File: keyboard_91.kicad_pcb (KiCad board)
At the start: 2 copper layers, 210 x 113 mm, 52 parts, among them J1 SW_Cherry_MX_1.00u_Plate, K1 SW_Cherry_MX_1.00u_Plate, M1 SW_Cherry_MX_1.00u_Plate, P1 SW_Cherry_MX_1.00u_Plate, Q1 SW_Cherry_MX_1.00u_Plate, T1 SW_Cherry_MX_1.00u_Plate, U1 SW_Cherry_MX_1.00u_Plate, X1 SW_Cherry_MX_1.00u_Plate, Y1 SW_Cherry_MX_1.00u_Plate

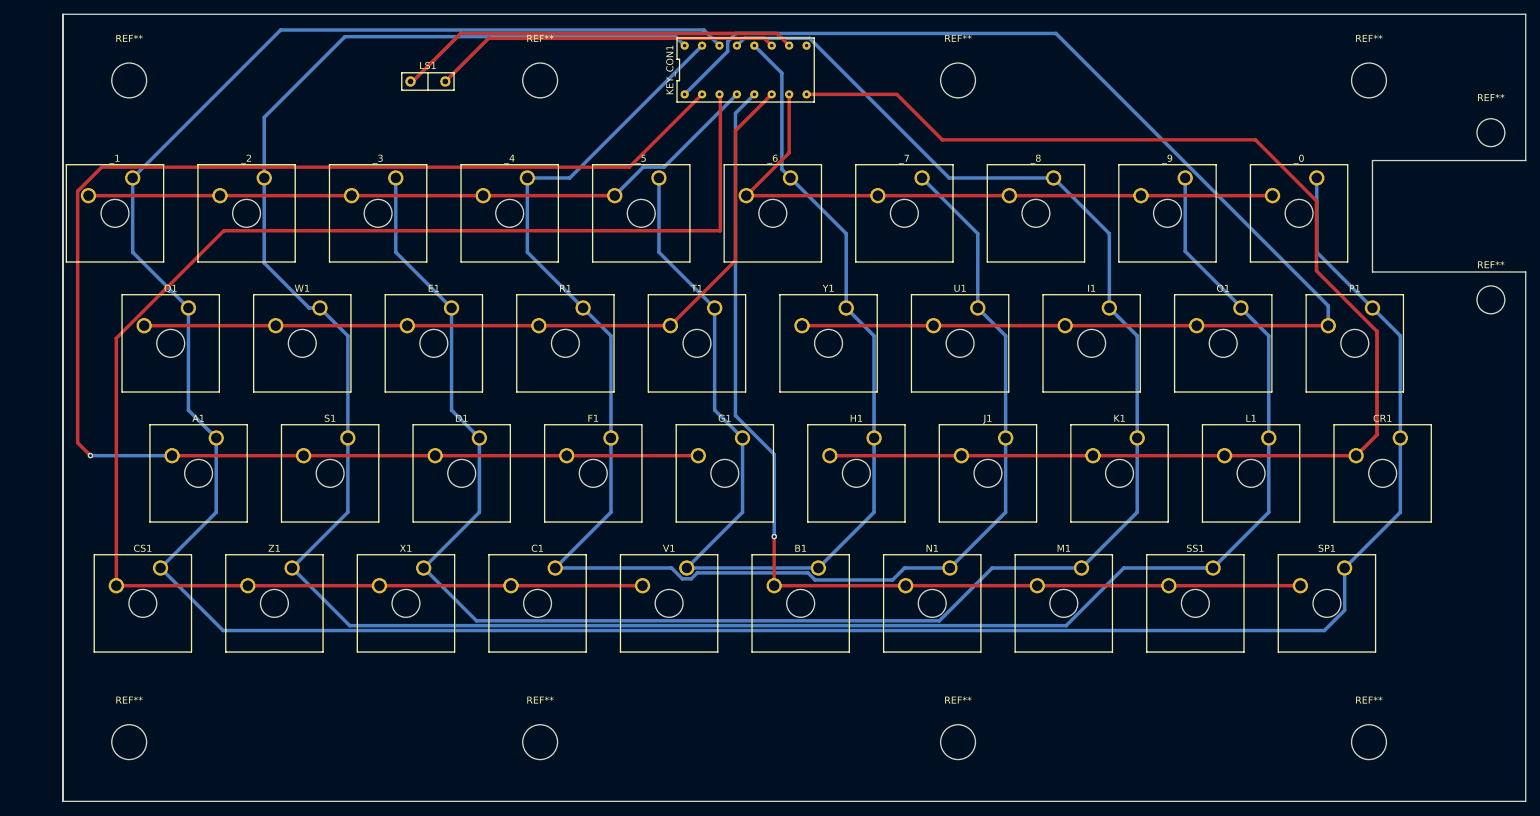
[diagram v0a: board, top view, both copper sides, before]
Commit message: Moure touches
- hide useless stuff
- add reset buttons SIP
- add speaker SIP
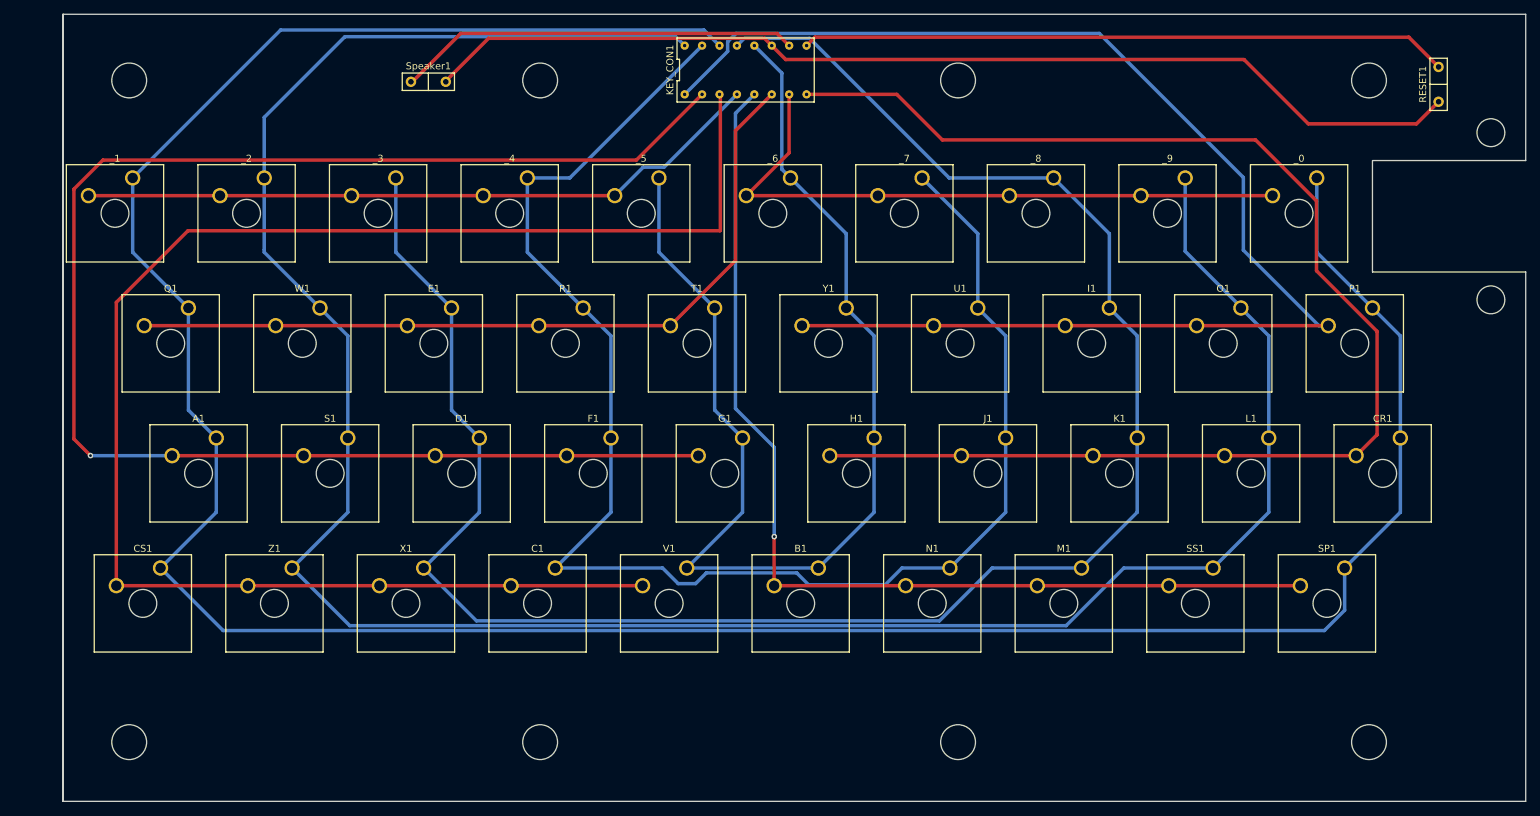
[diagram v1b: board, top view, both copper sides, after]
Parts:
- removed LS1: Speaker, Library:SIP-2
- added RESET1: RESET, Library:SIP-2, F.Cu at (217.5, 30.1)
- added Speaker1: Speaker, Library:SIP-2, F.Cu at (72.5, 29.7)
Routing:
- net /GND: track 49.9 -> 151.6 mm
- net /RST: track 0.00 -> 93.0 mm
- net /K_Y-P: track 191.4 -> 195.9 mm
- net /K_CS-V: track 223.8 -> 226.8 mm
- net /K_4-C_N-7: track 220.3 -> 221.5 mm
- net /K_A-G: track 221.4 -> 222.3 mm
- net /K_2-Z_SS-9: track 342.9 -> 342.0 mm
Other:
- board text added: "HC 85/90/91 Cherry MX PCB V1"
- board text added: "https://zx.licentia.eu"

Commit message: Second try
- fixed cherry mx holes (make them 0.8 mm)
- fixed connector holes
- fixed  sound & reset holes
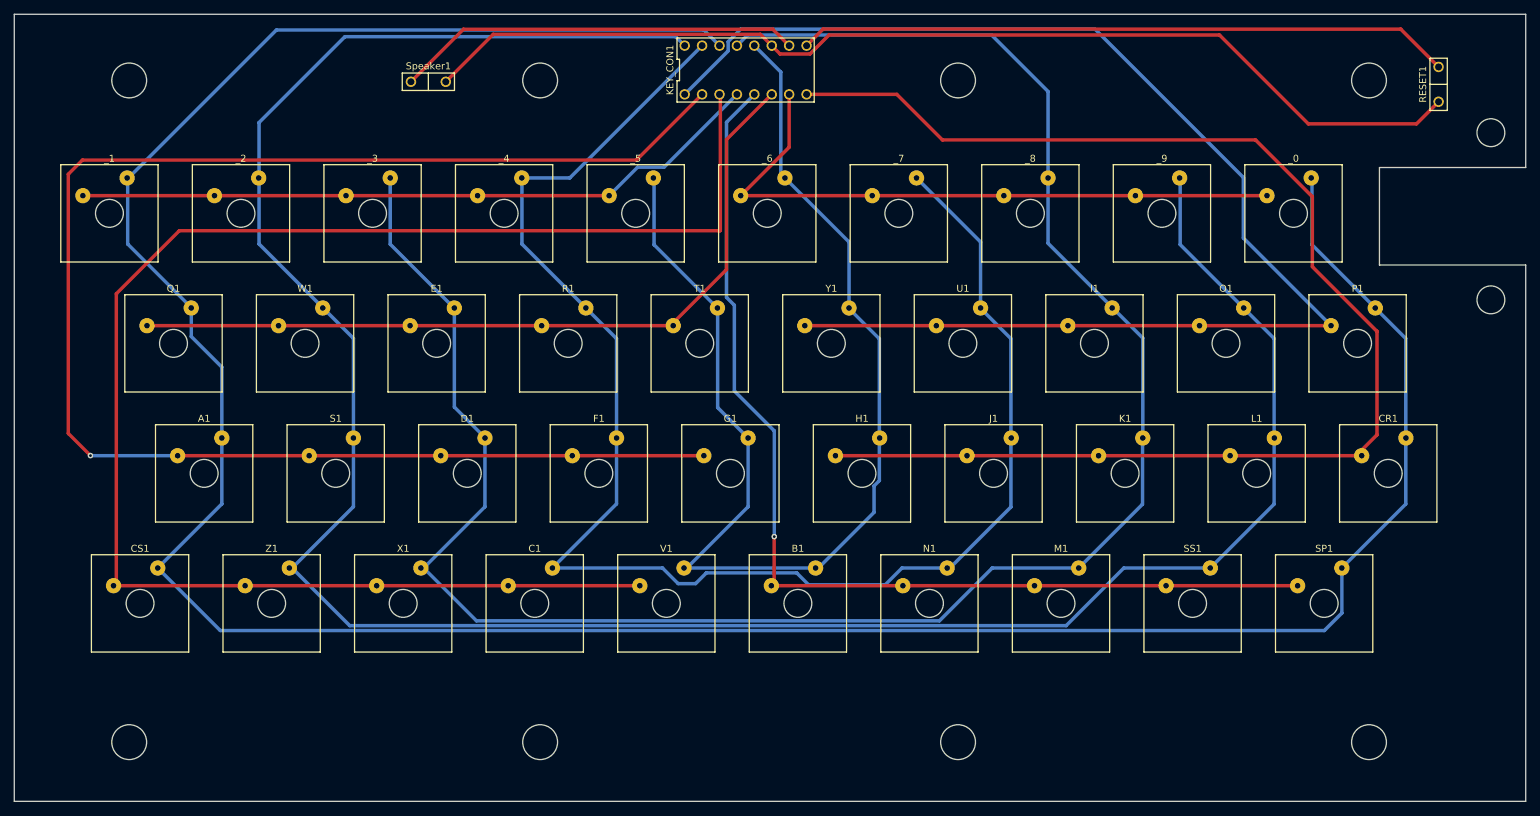
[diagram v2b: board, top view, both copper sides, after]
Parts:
- A1, B1, C1, CR1, CS1, D1, E1, F1, G1, H1, I1, J1, K1, L1, M1, N1, O1, P1, Q1, R1, S1, SP1, SS1, T1, U1, V1, W1, X1, Y1, Z1, _0, _1, _2, _3, _4, _5, _6, _7, _8, _9: value SW_Cherry_MX_1.00u_Plate -> SW_Cherry_MX_0.80u_Plate; footprint Button_Switch_Keyboard:SW_Cherry_MX_1.00u_Plate -> Library:SW_Cherry_MX_0.80u_Plate
- moved CR1 0.80 mm to (212.8, 80.8)
- moved H1 0.80 mm to (137.2, 80.8)
- moved J1 0.80 mm to (156.1, 80.8)
- moved _5 0.80 mm to (104.8, 43.5)
- moved _8 0.80 mm to (161.4, 43.5)
- moved _9 0.80 mm to (180.3, 43.5)
- moved _2 0.80 mm to (48.1, 43.5)
- moved _1 0.80 mm to (29.2, 43.5)
- moved A1 0.80 mm to (42.8, 80.8)
- moved D1 0.80 mm to (80.6, 80.8)
- moved F1 0.80 mm to (99.5, 80.8)
- moved G1 0.80 mm to (118.4, 80.8)
- moved S1 0.80 mm to (61.7, 80.8)
- moved _3 0.80 mm to (67.0, 43.5)
- moved _4 0.80 mm to (85.9, 43.5)
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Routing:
- net /K_3-X_M-8: track 283.5 -> 292.1 mm
- net /K_4-C_N-7: track 221.5 -> 224.8 mm
- net /K_1-CS_SP-0: track 403.5 -> 406.7 mm
- net /GND: track 151.6 -> 154.3 mm
- net /K_A-G: track 222.3 -> 224.7 mm
- net /K_2-Z_SS-9: track 342.0 -> 344.0 mm
- net /K_5-V_B_6: track 168.6 -> 170.2 mm
- net /K_6-0: track 92.6 -> 93.8 mm
- net /K_B_SP: track 149.5 -> 150.6 mm
- net /RST: track 93.0 -> 94.0 mm
- net /K_1-5: track 99.1 -> 99.9 mm
- net /K_CS-V: track 226.8 -> 227.5 mm
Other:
- board size 210 x 113 mm -> 217 x 113 mm
- board text added: "HC 85/90/91 Cherry MX PCB V2"
- board text removed: "HC 85/90/91 Cherry MX PCB V1"
